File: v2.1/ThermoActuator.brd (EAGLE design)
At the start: 99.1 x 80 mm, 78 parts, among them IC1 PCF8574T, IC2 ULN2003AD, IC3 REG1117, IC4 DS1307, Q1 200mA/50V, Q2 200mA/50V, Q3 MOSFET-NCHANNEL_DUAL, U1 CD74HCT4051_D_16, U2 AD5165BUJZ100-R2, U3 LTC4365CTS8TRMPBF

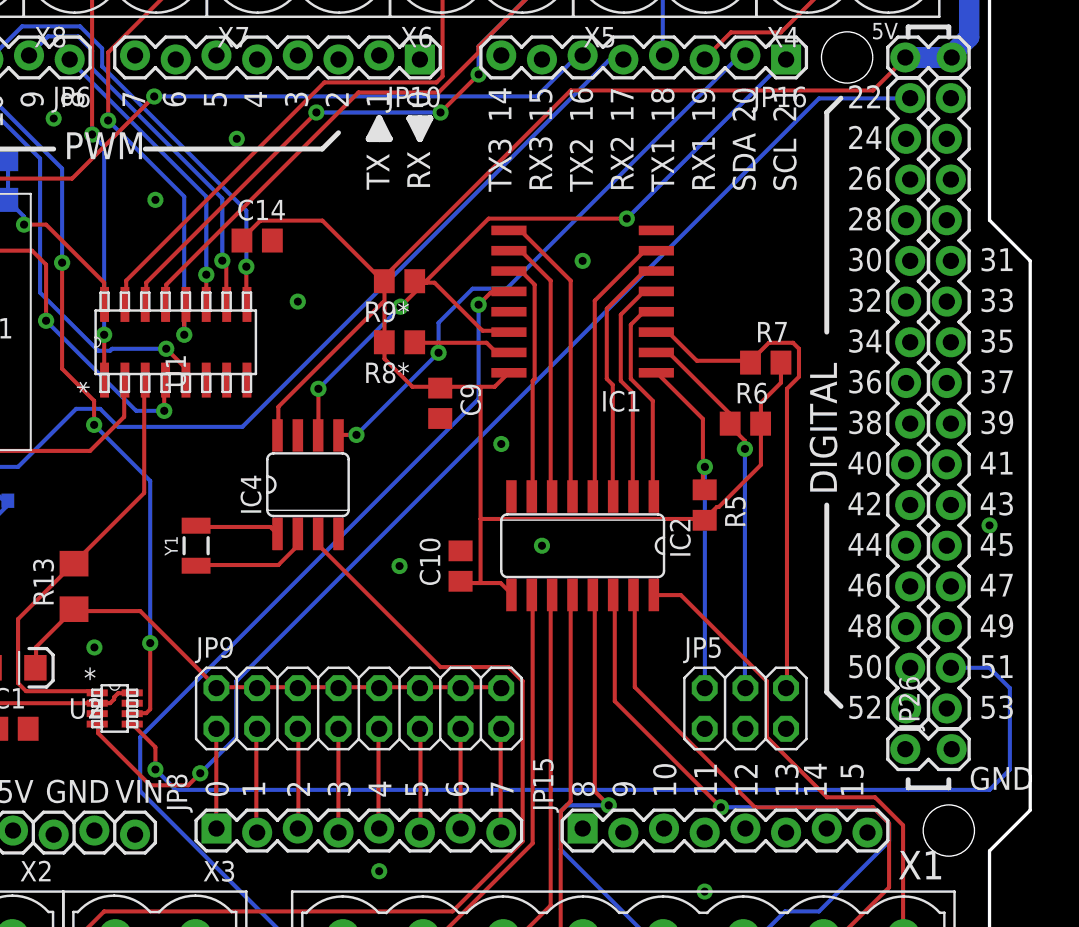
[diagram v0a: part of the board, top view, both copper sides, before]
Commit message: Digital Pot AD5165
apart from the simple support for the digital POT, it was
discovered that the double row header 38-pin was not correctly
pin-mapped on the shield. This caused the SPI CLK would be
connected to D22, instead of D52. Now, this is corrected, but...
too late:)
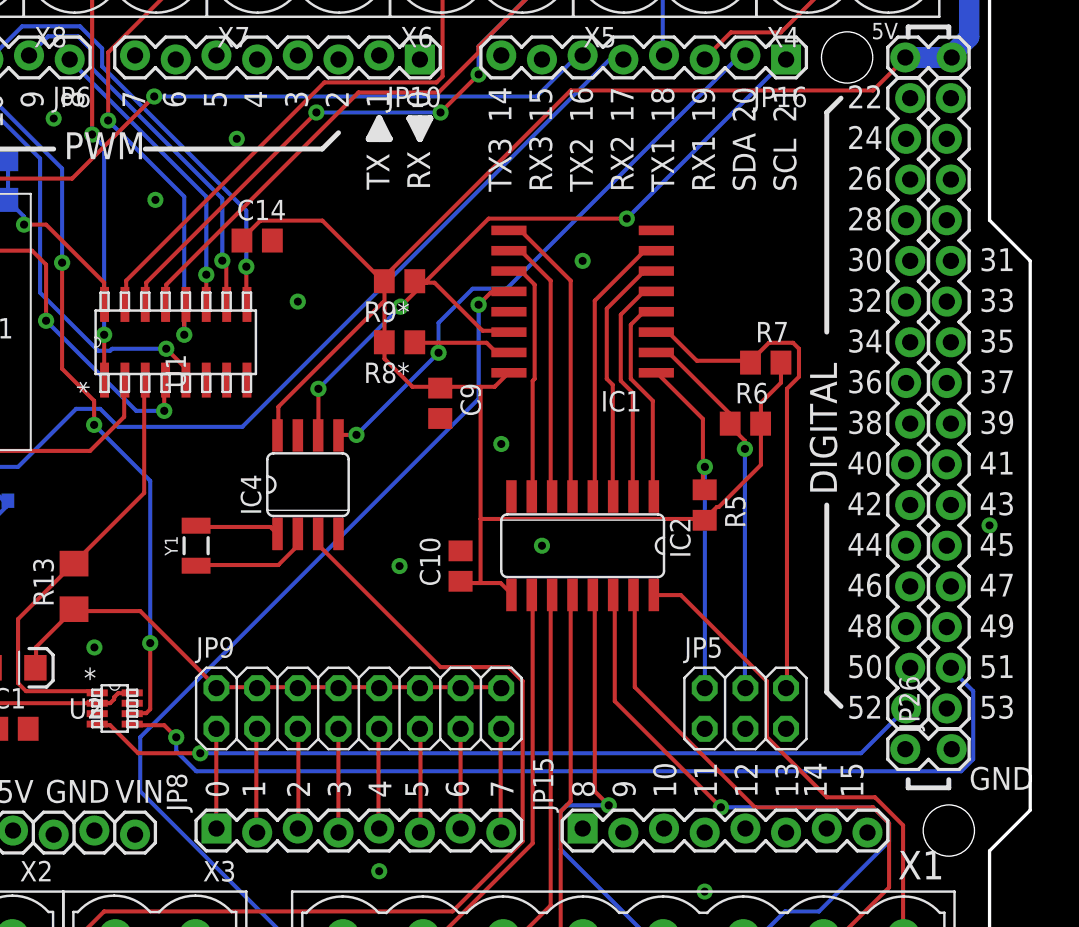
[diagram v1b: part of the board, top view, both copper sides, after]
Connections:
- net D22: now also JP27.16; no longer JP27.1
- net D24: now also JP27.15; no longer JP27.2
- net D26: now also JP27.14; no longer JP27.3
- net D28: now also JP27.13; no longer JP27.4
- net D30: now also JP27.12; no longer JP27.5
- net D32: now also JP27.11; no longer JP27.6
- net D34: now also JP27.10; no longer JP27.7
- net D36: now also JP27.9; no longer JP27.8
- net D38: now also JP27.8; no longer JP27.9
- net D40: now also JP27.7; no longer JP27.10
- net D42: now also JP27.6; no longer JP27.11
- net D44: now also JP27.5; no longer JP27.12
- net D46: now also JP27.4; no longer JP27.13
- net D48: now also JP27.3; no longer JP27.14
- net D50: now also JP27.2; no longer JP27.15
- net D52(SCLK): now also JP27.1; no longer JP27.16
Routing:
- net D52(SCLK): track 72.4 -> 52.4 mm
- net D51(MOSI): track 67.1 -> 60.8 mm
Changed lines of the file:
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@@
 </signal>
 <signal name="D22">
+<contactref element="JP27" pad="16"/>
+</signal>
+<signal name="D38">
+<contactref element="JP27" pad="8"/>
+</signal>
+<signal name="D40">
+<contactref element="JP27" pad="7"/>
+</signal>
+<signal name="D42">
+<contactref element="JP27" pad="6"/>
+</signal>
+<signal name="D44">
+<contactref element="JP27" pad="5"/>
+</signal>
+<signal name="D46">
+<contactref element="JP27" pad="4"/>
+</signal>
+<signal name="D48">
+<contactref element="JP27" pad="3"/>
+</signal>
+<signal name="D50">
+<contactref element="JP27" pad="2"/>
+</signal>
+<signal name="D52(SCLK)">
+<contactref element="U2" pad="4"/>
 <contactref element="JP27" pad="1"/>
-</signal>
-<signal name="D24">
-<contactref element="JP27" pad="2"/>
-</signal>
-<signal name="D26">
-<contactref element="JP27" pad="3"/>
-</signal>
-<signal name="D28">
-<contactref element="JP27" pad="4"/>
-</signal>
-<signal name="D30">
-<contactref element="JP27" pad="5"/>
-</signal>
-<signal name="D32">
-<contactref element="JP27" pad="6"/>
-</signal>
-<signal name="D34">
-<contactref element="JP27" pad="7"/>
-</signal>
-<signal name="D36">
-<contactref element="JP27" pad="8"/>
-</signal>
-<signal name="D38">
-<contactref element="JP27" pad="9"/>
-</signal>
-<signal name="D40">
-<contactref element="JP27" pad="10"/>
-</signal>
-<signal name="D42">
-<contactref element="JP27" pad="11"/>
-</signal>
-<signal name="D44">
-<contactref element="JP27" pad="12"/>
-</signal>
-<signal name="D46">
-<contactref element="JP27" pad="13"/>
-</signal>
-<signal name="D48">
-<contactref element="JP27" pad="14"/>
-</signal>
-<signal name="D50">
-<contactref element="JP27" pad="15"/>
-</signal>
-<signal name="D52(SCLK)">
-<contactref element="JP27" pad="16"/>
-<contactref element="U2" pad="4"/>
-<wire x1="40.875" y1="25.125" x2="40.875" y2="25.625" width="0.254" layer="1"/>
-<wire x1="44.125" y1="21.875" x2="40.875" y2="25.125" width="0.254" layer="1"/>
-<wire x1="46.5" y1="21.875" x2="44.125" y2="21.875" width="0.254" layer="1"/>
-<wire x1="47.25" y1="22.625" x2="46.5" y2="21.875" width="0.254" layer="1"/>
-<wire x1="49.5" y1="24.875" x2="47.25" y2="22.625" width="0.254" layer="16"/>
-<wire x1="49.5" y1="28.375" x2="49.5" y2="24.875" width="0.254" layer="16"/>
-<wire x1="85.875" y1="64.75" x2="49.5" y2="28.375" width="0.254" layer="16"/>
-<wire x1="91.5" y1="64.75" x2="85.875" y2="64.75" width="0.254" layer="16"/>
+<wire x1="41.625" y1="25.625" x2="40.875" y2="25.625" width="0.254" layer="1"/>
+<wire x1="43.375" y1="23.875" x2="41.625" y2="25.625" width="0.254" layer="1"/>
+<wire x1="47.25" y1="23.875" x2="43.375" y2="23.875" width="0.254" layer="1"/>
+<wire x1="88.5" y1="23.875" x2="47.25" y2="23.875" width="0.254" layer="16"/>
+<wire x1="91.25" y1="26.625" x2="88.5" y2="23.875" width="0.254" layer="16"/>
 <wire x1="40.875" y1="25.625" x2="40.8178" y2="25.694996875" width="0.254" layer="1"/>
-<wire x1="91.5" y1="64.75" x2="91.567" y2="64.77" width="0.254" layer="16"/>
-<via x="47.25" y="22.625" extent="1-16" drill="0.508"/>
+<wire x1="91.25" y1="26.625" x2="91.313" y2="26.67" width="0.254" layer="16"/>
+<via x="47.25" y="23.875" extent="1-16" drill="0.508"/>
 </signal>
 <signal name="D25">
@@
 <contactref element="JP26" pad="2"/>
 <contactref element="U2" pad="5"/>
-<wire x1="43.0022" y1="25.694996875" x2="44.45" y2="24.247196875" width="0.254" layer="1"/>
-<wire x1="44.45" y1="24.247196875" x2="44.45" y2="22.86" width="0.254" layer="1"/>
-<via x="44.45" y="22.86" extent="1-16" drill="0.5"/>
-<wire x1="44.45" y1="22.86" x2="45.72" y2="21.59" width="0.254" layer="16"/>
-<wire x1="45.72" y1="21.59" x2="96.52" y2="21.59" width="0.254" layer="16"/>
-<wire x1="96.52" y1="21.59" x2="97.79" y2="22.86" width="0.254" layer="16"/>
-<wire x1="97.79" y1="22.86" x2="97.79" y2="27.94" width="0.254" layer="16"/>
-<wire x1="97.79" y1="27.94" x2="96.52" y2="29.21" width="0.254" layer="16"/>
-<wire x1="96.52" y1="29.21" x2="94.107" y2="29.21" width="0.254" layer="16"/>
+<wire x1="45" y1="25.625" x2="43.125" y2="25.625" width="0.254" layer="1"/>
+<wire x1="45.75" y1="24.875" x2="45" y2="25.625" width="0.254" layer="1"/>
+<wire x1="45.75" y1="24" x2="45.75" y2="24.875" width="0.254" layer="16"/>
+<wire x1="47" y1="22.75" x2="45.75" y2="24" width="0.254" layer="16"/>
+<wire x1="94.75" y1="22.75" x2="47" y2="22.75" width="0.254" layer="16"/>
+<wire x1="95.5" y1="23.5" x2="94.75" y2="22.75" width="0.254" layer="16"/>
+<wire x1="95.5" y1="27.75" x2="95.5" y2="23.5" width="0.254" layer="16"/>
+<wire x1="94.125" y1="29.125" x2="95.5" y2="27.75" width="0.254" layer="16"/>
+<wire x1="43.125" y1="25.625" x2="43.0022" y2="25.694996875" width="0.254" layer="1"/>
+<wire x1="94.125" y1="29.125" x2="94.107" y2="29.21" width="0.254" layer="16"/>
+<via x="45.75" y="24.875" extent="1-16" drill="0.508"/>
 </signal>
 <signal name="D53">
@@
 <contactref element="JP8" pad="1"/>
 <contactref element="JP9" pad="1"/>
-<wire x1="48.25" y1="19.25" x2="48.25" y2="25.375" width="0.254" layer="1"/>
 <wire x1="48.25" y1="25.375" x2="48.26" y2="25.4" width="0.254" layer="1"/>
 <wire x1="48.25" y1="19.25" x2="48.26" y2="19.177" width="0.254" layer="1"/>
+<wire x1="48.25" y1="19.375" x2="48.25" y2="25.25" width="0.254" layer="1"/>
+<wire x1="48.25" y1="25.25" x2="48.26" y2="25.4" width="0.254" layer="1"/>
+<wire x1="48.25" y1="19.375" x2="48.26" y2="19.177" width="0.254" layer="1"/>
 </signal>
 <signal name="N$27">
@@
 <signal name="N$52">
 </signal>
+<signal name="D24">
+<contactref element="JP27" pad="15"/>
+</signal>
+<signal name="D26">
+<contactref element="JP27" pad="14"/>
+</signal>
+<signal name="D28">
+<contactref element="JP27" pad="13"/>
+</signal>
+<signal name="D30">
+<contactref element="JP27" pad="12"/>
+</signal>
+<signal name="D32">
+<contactref element="JP27" pad="11"/>
+</signal>
+<signal name="D34">
+<contactref element="JP27" pad="10"/>
+</signal>
+<signal name="D36">
+<contactref element="JP27" pad="9"/>
+</signal>
 </signals>
